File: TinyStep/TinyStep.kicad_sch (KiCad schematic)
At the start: 2 parts, among them U1 ATtiny204-SS

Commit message: this might work
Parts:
- added A1: Pololu_Breakout_A4988, Module:Pololu_Breakout-16_15.2x20.3mm, symbol Driver_Motor:Pololu_Breakout_A4988
- added C2: 100uF 50V, Capacitor_THT:CP_Radial_D8.0mm_P3.50mm, symbol Device:C_Polarized
- added J1: Conn_01x03_Pin, Connector_PinHeader_2.54mm:PinHeader_1x03_P2.54mm_Vertical, symbol Connector:Conn_01x03_Pin
- added J2: Conn_01x04_Pin, Connector_JST:JST_XH_S4B-XH-A_1x04_P2.50mm_Horizontal, symbol Connector:Conn_01x04_Pin
- added J3, J4, J5, J6: Conn_01x02_Pin, Connector_PinHeader_2.54mm:PinHeader_1x02_P2.54mm_Vertical, symbol Connector:Conn_01x02_Pin
- added J7: Barrel_Jack_Switch, Connector_BarrelJack:BarrelJack_Wuerth_6941xx301002, symbol Connector:Barrel_Jack_Switch
- added R1, R2, R3, R4, R5, R6, R7: 10k, Resistor_SMD:R_0805_2012Metric_Pad1.20x1.40mm_HandSolder, symbol Device:R
- added SW1: SW_DIP_x03, Button_Switch_SMD:SW_DIP_SPSTx03_Slide_Omron_A6S-310x_W8.9mm_P2.54mm, symbol Switch:SW_DIP_x03
- C1: value C -> 100n; footprint Capacitor_THT:C_Disc_D5.0mm_W2.5mm_P5.00mm -> Capacitor_SMD:C_0805_2012Metric_Pad1.18x1.45mm_HandSolder
- U1: footprint BREAKOUT:DIP-16_SOIC_BREAKOUT -> Package_SO:SOIC-14_3.9x8.7mm_P1.27mm
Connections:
- net VCC: now also A1.13 (~{RESET}), A1.14 (~{SLEEP}), A1.2 (VDD), J1.2 (Pin_2), R4.2, R5.2, R6.2, R7.2, SW1.1, SW1.2, SW1.3
- net GND: now reaches C1.1, U1.14 (GND)
- net GND: now also A1.1 (GND), A1.7 (GND), C2.2, J1.3 (Pin_3), J7.2, J7.3, R1.1, R2.1, R3.1
- net UPDI: now reaches U1.10 (~{RESET}/PA0)
- net UPDI: now also J1.1 (Pin_1)
- net A1_DI: now reaches U1.11 (PA1)
- net A1_DI: now also A1.16 (DIR)
- net A1_ST: now reaches U1.12 (PA2)
- net A1_ST: now also A1.15 (STEP)
- net A1_EN: now reaches U1.13 (PA3)
- net A1_EN: now also A1.9 (~{ENABLE})
- net BTN0: now reaches U1.2 (PA4)
- net BTN0: now also J3.1 (Pin_1)
- net BTN1: now reaches U1.3 (PA5)
- net BTN1: now also J4.1 (Pin_1)
- net BTN3: now reaches U1.4 (PA6)
- net BTN3: now also J6.1 (Pin_1)
- net BTN2: now reaches U1.5 (PA7)
- net BTN2: now also J5.1 (Pin_1)
- new net: A1.11 (MS2), R2.2, SW1.5
- new net: J5.2 (Pin_2), R6.1
- new net: A1.12 (MS3), R1.2, SW1.6
- new net: J4.2 (Pin_2), R5.1
- new net: A1.3 (1B), J2.1 (Pin_1)
- new net: A1.4 (1A), J2.2 (Pin_2)
- new net: A1.5 (2A), J2.3 (Pin_3)
- new net: A1.6 (2B), J2.4 (Pin_4)
- new net: J3.2 (Pin_2), R4.1
- new net: J6.2 (Pin_2), R7.1
- new net: A1.10 (MS1), R3.2, SW1.4
- new net +12V: A1.8 (VMOT), C2.1, J7.1
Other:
- moved on the sheet: C1, U1

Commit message: v0.1
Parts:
- removed A1: Pololu_Breakout_A4988, Module:Pololu_Breakout-16_15.2x20.3mm, symbol Driver_Motor:Pololu_Breakout_A4988
- removed J3, J4, J5, J6: Conn_01x02_Pin, Connector_PinHeader_2.54mm:PinHeader_1x02_P2.54mm_Vertical, symbol Connector:Conn_01x02_Pin
- removed R5, R6, R7: 10k, Resistor_SMD:R_0805_2012Metric_Pad1.20x1.40mm_HandSolder, symbol Device:R
- removed SW1: SW_DIP_x03, Button_Switch_SMD:SW_DIP_SPSTx03_Slide_Omron_A6S-310x_W8.9mm_P2.54mm, symbol Switch:SW_DIP_x03
- added A2: ~, Module_TMC2209_BTT:TMC2209_BTT, symbol Driver_Motor_TMC2209_BTT:TMC2209_BTT
- added C3: 10uF, Capacitor_SMD:C_0805_2012Metric_Pad1.18x1.45mm_HandSolder, symbol Device:C
- added C4: 100nF, Capacitor_SMD:C_0805_2012Metric_Pad1.18x1.45mm_HandSolder, symbol Device:C
- added C5, C6: 22uF, Capacitor_SMD:C_0805_2012Metric_Pad1.18x1.45mm_HandSolder, symbol Device:C
- added J4: Conn_02x05_Odd_Even, Connector_PinHeader_2.54mm:PinHeader_2x05_P2.54mm_Vertical, symbol Connector_Generic:Conn_02x05_Odd_Even
- added J5: Conn_02x02_Odd_Even, Connector_PinHeader_2.54mm:PinHeader_2x02_P2.54mm_Vertical, symbol Connector_Generic:Conn_02x02_Odd_Even
- added JP1: SolderJumper_3_Bridged12, Jumper:SolderJumper-3_P1.3mm_Bridged12_RoundedPad1.0x1.5mm_NumberLabels, symbol Jumper:SolderJumper_3_Bridged12
- added JP2, JP3, JP4: SolderJumper_2_Open, Jumper:SolderJumper-2_P1.3mm_Open_RoundedPad1.0x1.5mm, symbol Jumper:SolderJumper_2_Open
- added L1: 4.7uH, Inductor_SMD:L_0805_2012Metric_Pad1.15x1.40mm_HandSolder, symbol Device:L
- added U2: AP63205WU, Package_TO_SOT_SMD:TSOT-23-6, symbol Regulator_Switching:AP63205WU
- C1: value 100n -> 100nF
- C2: value 100uF 50V -> 47uF 50V; footprint Capacitor_THT:CP_Radial_D8.0mm_P3.50mm -> Capacitor_SMD:CP_Elec_6.3x7.7
- R4: value 10k -> 1k
- renumbered J7 to J3
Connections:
- net +12V: now also A2.16 (VMOT), C3.1, J5.3 (Pin_3), U2.2 (EN), U2.3 (IN)
- net A1_DI: now also U1.3 (PA5), A2.8 (DIR); no longer U1.11 (PA1)
- net A1_EN: now also A2.1 (EN)
- net A1_ST: now also U1.2 (PA4), A2.7 (STEP); no longer U1.12 (PA2)
- net BTN0: now also U1.4 (PA6), J4.1 (Pin_1); no longer U1.2 (PA4)
- net BTN1: now also U1.5 (PA7), J4.3 (Pin_3); no longer U1.3 (PA5)
- net BTN2: now also U1.11 (PA1), J4.5 (Pin_5); no longer U1.5 (PA7)
- net BTN3: now also U1.9 (PB0), J4.7 (Pin_7); no longer U1.4 (PA6)
- net GND: now also C1.2, A2.15 (GND), A2.9 (GND), C3.2, C5.2, C6.2, J4.10 (Pin_10), J4.2 (Pin_2), J4.4 (Pin_4), J4.6 (Pin_6), J4.8 (Pin_8), J5.2 (Pin_2), J5.4 (Pin_4), U2.4 (GND); no longer C1.1
- net VCC: now also C1.1, A2.10 (VCC), C5.1, C6.1, J5.1 (Pin_1), JP2.2 (B), JP3.2 (B), JP4.2 (B), L1.2, U2.1 (FB); no longer C1.2, R4.2
- net at R2.2: now also A2.3 (MS2), JP3.1 (A)
- net A1_MS3_UART: now reaches U1.6 (PB3)
- net A1_MS3_UART: now also R4.2, JP1.3 (B)
- net USART_Tx: now reaches U1.7 (PB2)
- net USART_Tx: now also R4.1
- net BTN4: now reaches U1.8 (PB1)
- net BTN4: now also J4.9 (Pin_9)
- net at R1.2: now also A2.2 (MS1), JP4.1 (A)
- net at J2.1 (Pin_1): now also A2.11 (B2)
- net at J2.2 (Pin_2): now also A2.12 (B1)
- net at J2.3 (Pin_3): now also A2.13 (A1)
- net at J2.4 (Pin_4): now also A2.14 (A2)
- net A1_MS3_SW: now reaches R3.2
- net A1_MS3_SW: now also JP1.1 (A), JP2.1 (A)
- new net: C4.1, L1.1, U2.5 (SW)
- new net: C4.2, U2.6 (BST)
- new net A1_DIAG: A2.17 (DIAG), U1.12 (PA2)
- new net A1_MS3: A2.4 (MS3/UART), JP1.2 (C)
- new net A1_RST: A2.5 (RST/UART)
- new net A1_SLP: A2.6 (SLP/CLK)
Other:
- moved on the sheet: C1, C2, J1, J2, J3, R1, R2, R3, U1

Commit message: GND vias, cleaner board
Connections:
- net A1_MS3_SW: now also JP1.3 (B); no longer JP1.1 (A)
- net A1_MS3_UART: now also JP1.1 (A); no longer JP1.3 (B)

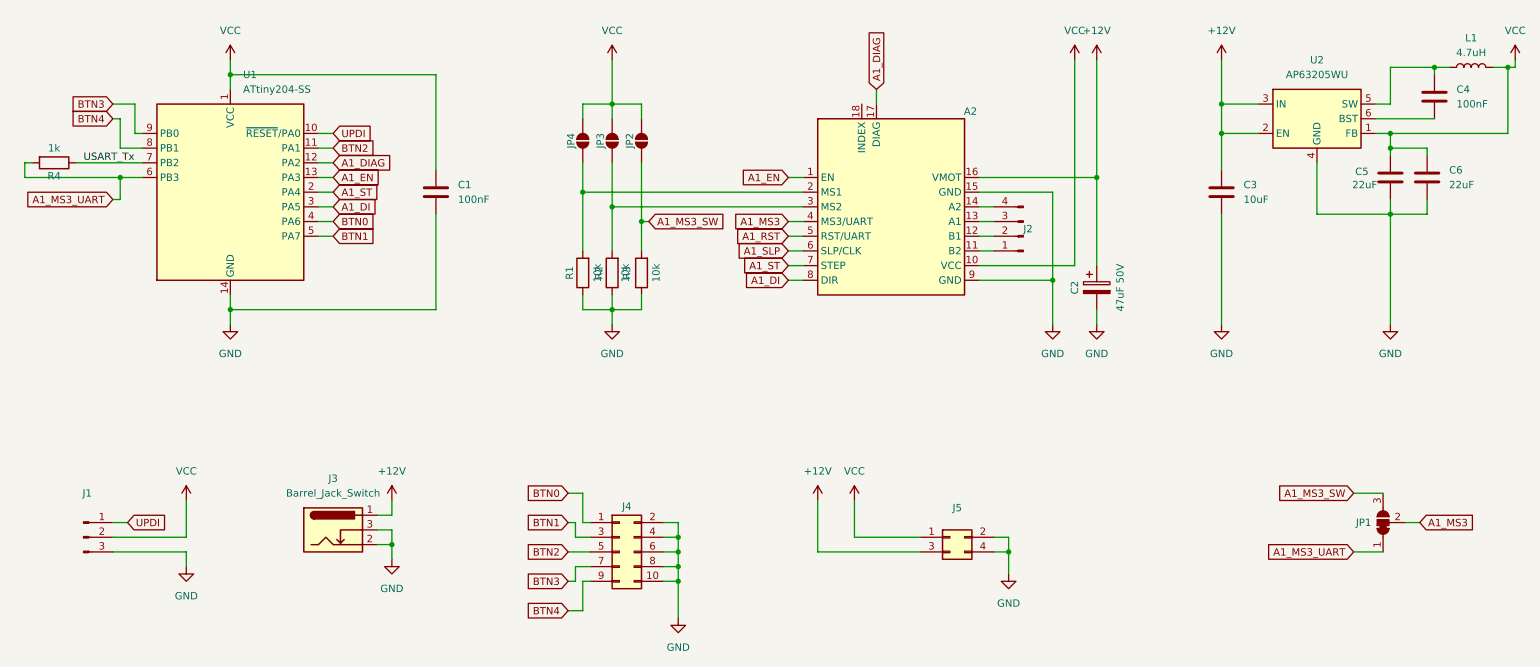
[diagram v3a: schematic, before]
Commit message: HT42B534 library
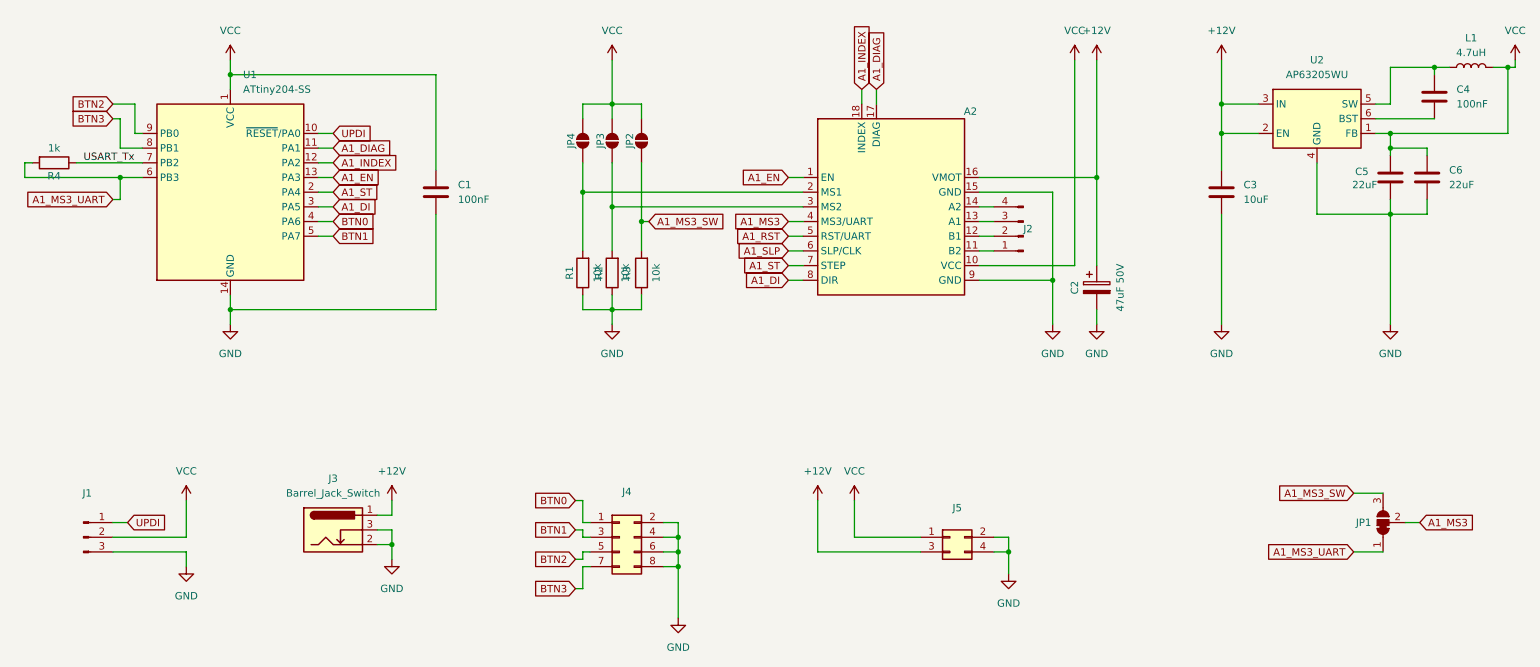
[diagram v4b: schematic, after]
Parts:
- J4: value Conn_02x05_Odd_Even -> Conn_02x04_Odd_Even; footprint Connector_PinHeader_2.54mm:PinHeader_2x05_P2.54mm_Vertical -> Connector_PinHeader_2.54mm:PinHeader_2x04_P2.54mm_Vertical; symbol Connector_Generic:Conn_02x05_Odd_Even -> Connector_Generic:Conn_02x04_Odd_Even
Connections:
- net A1_DIAG: now also U1.11 (PA1); no longer U1.12 (PA2)
- net BTN2: now also U1.9 (PB0); no longer U1.11 (PA1)
- net BTN3: now also U1.8 (PB1); no longer U1.9 (PB0)
- net GND: no longer J4.10 (Pin_10)
- net A1_INDEX: now reaches A2.18 (INDEX)
- net A1_INDEX: now also U1.12 (PA2)
- removed net BTN4: J4.9 (Pin_9), U1.8 (PB1)
